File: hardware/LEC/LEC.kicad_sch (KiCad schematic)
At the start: 32 parts, among them J1 54-00278, J10 Conn_01x02, J11 54-00278, J12 54-00278, J13 54-00278, J2 54-00278, J3 54-00278, J4 54-00278, J5 54-00278, J6 54-00278, J7 54-00278, J8 54-00278, J9 54-00278, J9 Conn_01x02, U1 Pico, U15 MCP3564RT-E/ST, U3 MC7809CTG, U4 W25Q128JVSIQ, U5 MAX31855KASA, U6 MAX31855KASA, U7 L7805

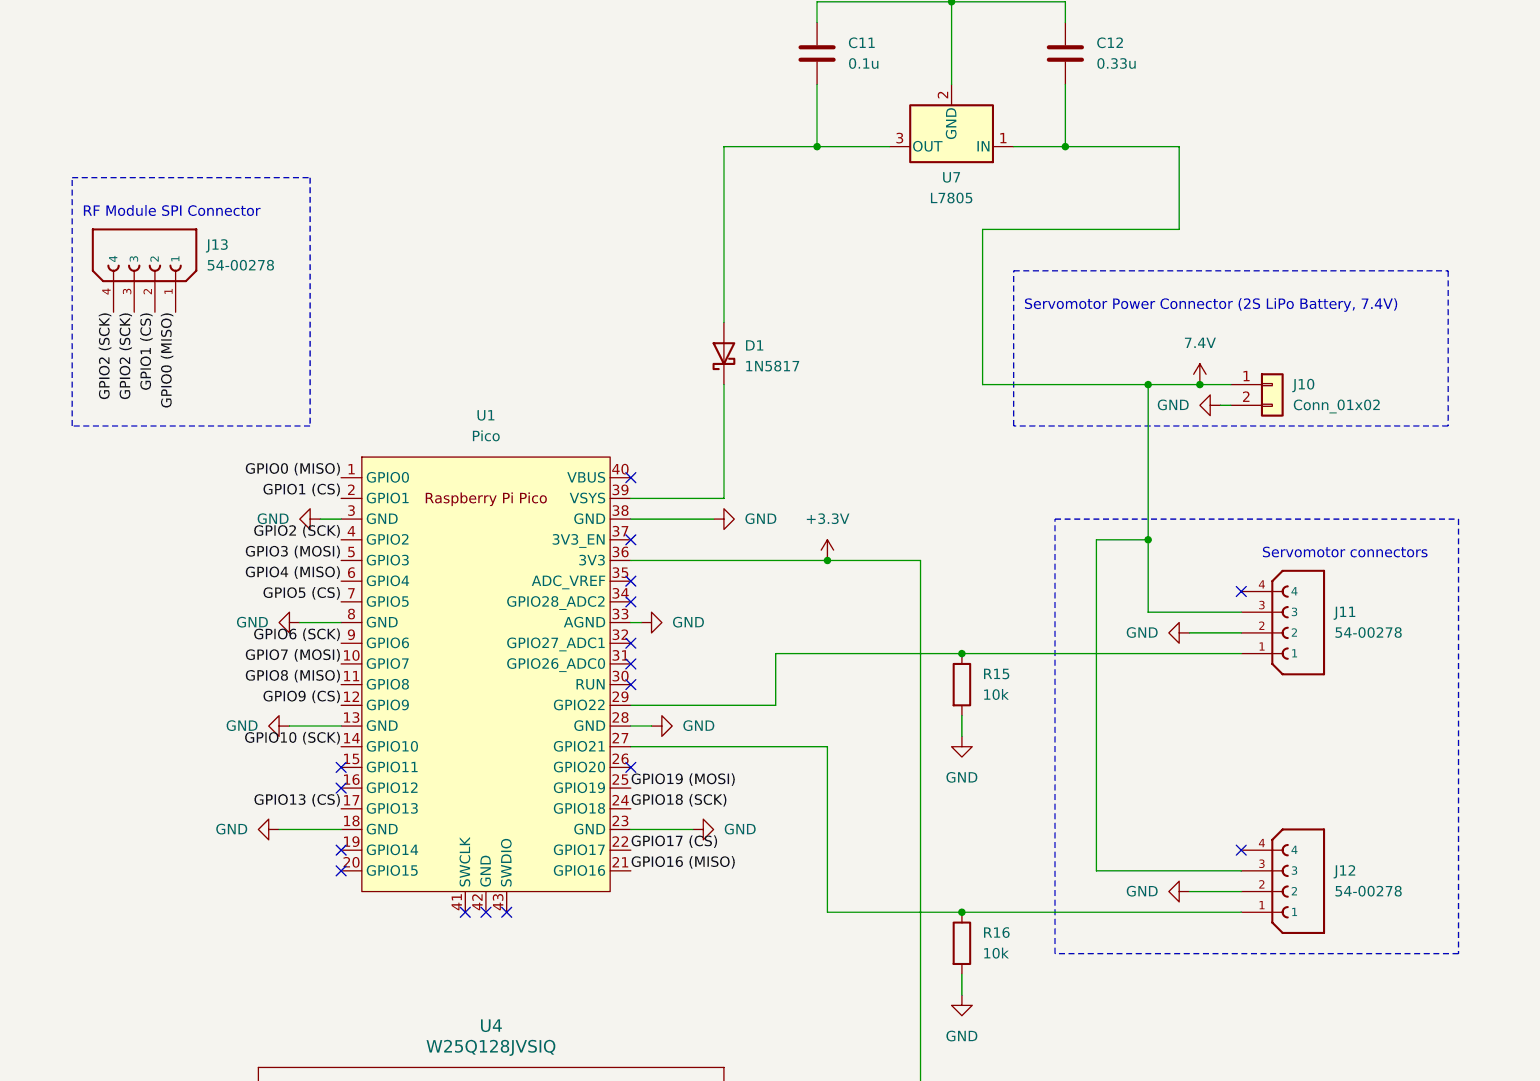
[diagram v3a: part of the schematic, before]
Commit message: Added bulk capacitors to ADC LVRs, servos, and pico power inputs
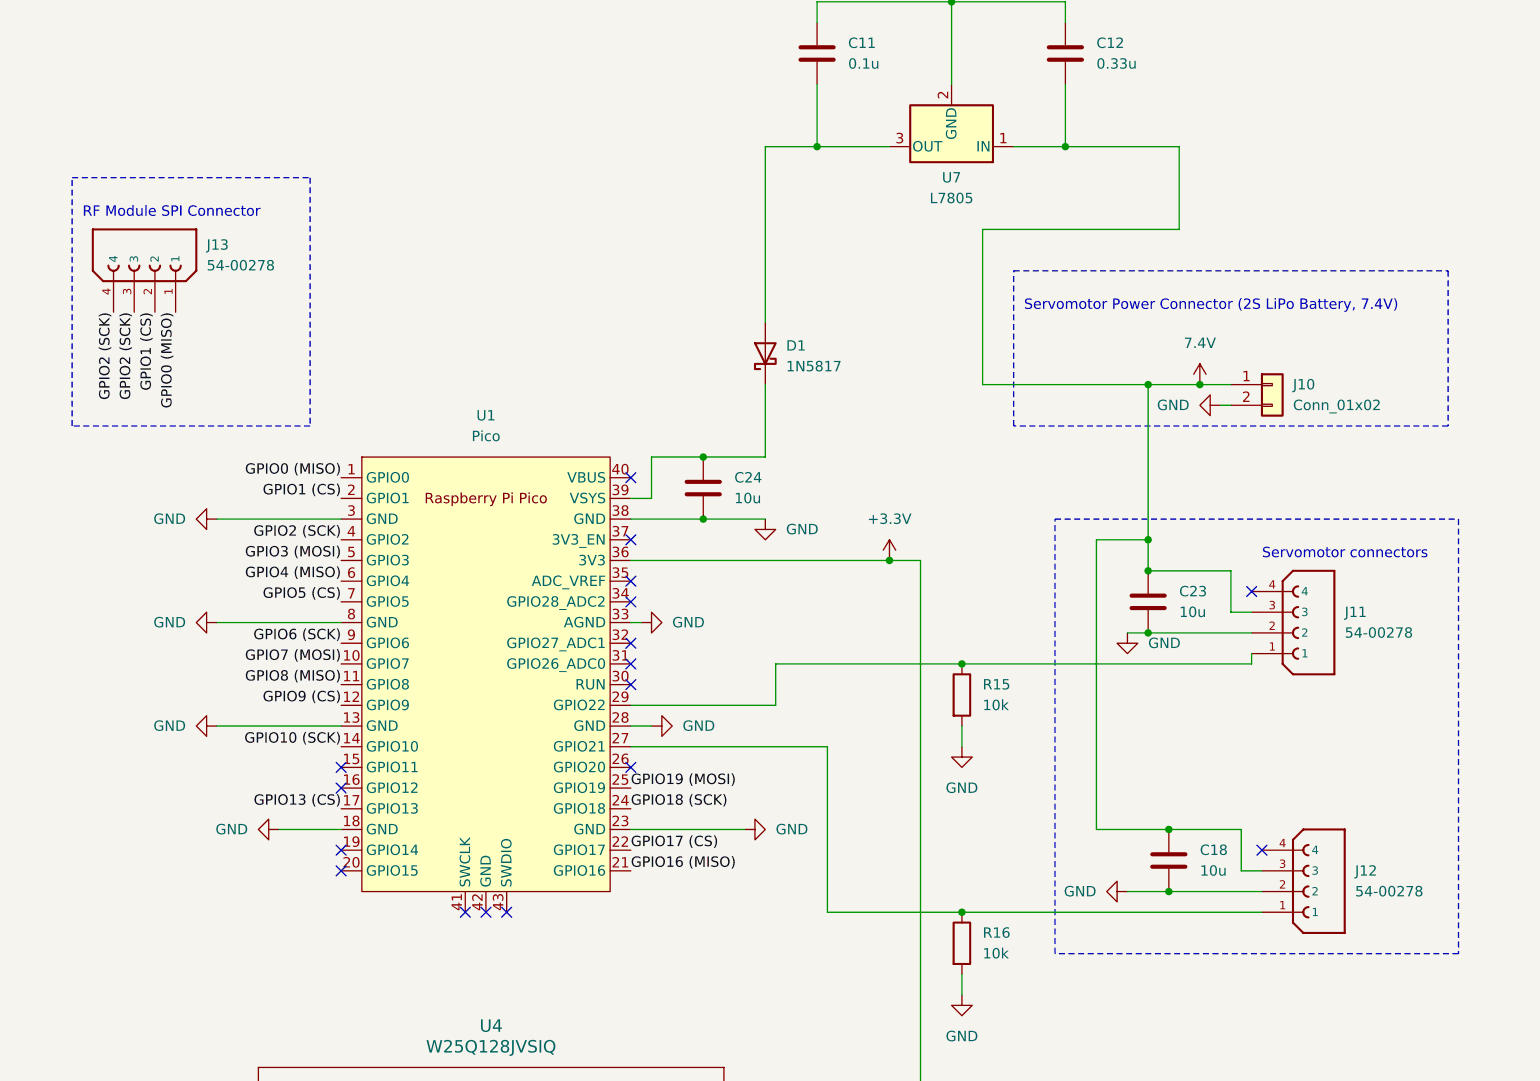
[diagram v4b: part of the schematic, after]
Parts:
- added C18, C23, C24: 10u, symbol Device:C
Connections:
- net +12V: now also C18.1, C23.1
- net GND: now also C18.2, C23.2, C24.2
- net at D1.1 (K), U1.39 (VSYS): now also C24.1
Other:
- moved on the sheet: D1, J11, J12, R15

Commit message: Schematic done
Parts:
- removed C1 (x2): 100n, Capacitor_SMD:C_1206_3216Metric, symbol Device:C
- removed C11: 0.1u, symbol Device:C
- removed C12: 0.33u, symbol Device:C
- removed C23: 10u, symbol Device:C
- removed J9: 54-00278, TENSILITY_54-00278, symbol 4_Pin_M8_Socket_Female:54-00278
- removed R15, R16: 10k, symbol Device:R
- added C1 (x2): 100n, Capacitor_SMD:C_0603_1608Metric, symbol Device:C
- added C21, C22, C25: 10u, Capacitor_SMD:C_0805_2012Metric, symbol Device:C
- added J14: 54-00278, M8Connector:TENSILITY_54-00278, symbol 4_Pin_M8_Socket_Female:54-00278
- added R3 (x2): 10K, Resistor_SMD:R_0603_1608Metric, symbol Device:R_US
- C1: footprint Capacitor_SMD:C_1206_3216Metric -> Capacitor_SMD:C_0603_1608Metric; Digikey https://www.digikey.com/en/products/detail/murata-electroni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 -> https://www.digikey.com/en/products/detail/samsung-electro-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
- C14, C18, C24: footprint (none) -> Capacitor_SMD:C_0805_2012Metric; DigiKey (none) -> https://www.digikey.com/en/products/detail/samsung-electro-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
- C19, C20: value 0.33u -> 10u; footprint (none) -> Capacitor_SMD:C_0805_2012Metric; DigiKey (none) -> https://www.digikey.com/en/products/detail/samsung-electro-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
- J1, J11, J12, J13, J2, J3, J4, J5, J6, J7, J8: footprint TENSILITY_54-00278 -> M8Connector:TENSILITY_54-00278; DigiKey (none) -> https://www.digikey.com/en/products/detail/tensility-intern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
- J10, J9: footprint (none) -> Connector_AMASS:AMASS_XT30UPB-M_1x02_P5.0mm_Vertical
- U1: footprint RPi_Pico:RPi_Pico_SMD_TH -> RPiPico:RPi_Pico_SMD_TH; DigiKey (none) -> https://www.digikey.com/en/products/detail/raspberry-pi/SC0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
- U15: footprint TSSOP20_ST_MCH -> MCP3564R/T:TSSOP20_ST_MCH
- U3: footprint TO-220AB_ONS -> MC7809CTG:TO-220AB_ONS
- U4: footprint SOIC_128JVSIQ_WIN -> W25Q128JVSIQ:SOIC_128JVSIQ_WIN
- U7: footprint (none) -> L7805CV:TO-220_STM; DigiKey (none) -> https://www.digikey.com/en/products/detail/stmicroelectroni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
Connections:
- net +12V: now also J10.2 (Pin_2), C22.1, C25.2; no longer J10.1 (Pin_1)
- net +3.3V: now also C1.1, C1.2
- net ADC_Power_Circuit/VIN: now also J9.2 (Pin_2); no longer J9.1 (Pin_1)
- net GND: now also J10.1 (Pin_1), J9.1 (Pin_1), U1.42 (GND), C1.1, C1.2, C21.1, C22.2, C25.1, R3.2, R3.2; no longer J10.2 (Pin_2), J9.2 (Pin_2)
- net at J12.1, U1.27 (GPIO21): now also R3.1
- net at J11.1, U1.29 (GPIO22): now also R3.1
- net at D1.2 (A), U7.3 (OUT): now also C21.2
- net at U5.3 (T+): now also J14.1
- net at U5.2 (T-): now also J14.2
- no-connect marks 24 -> 23

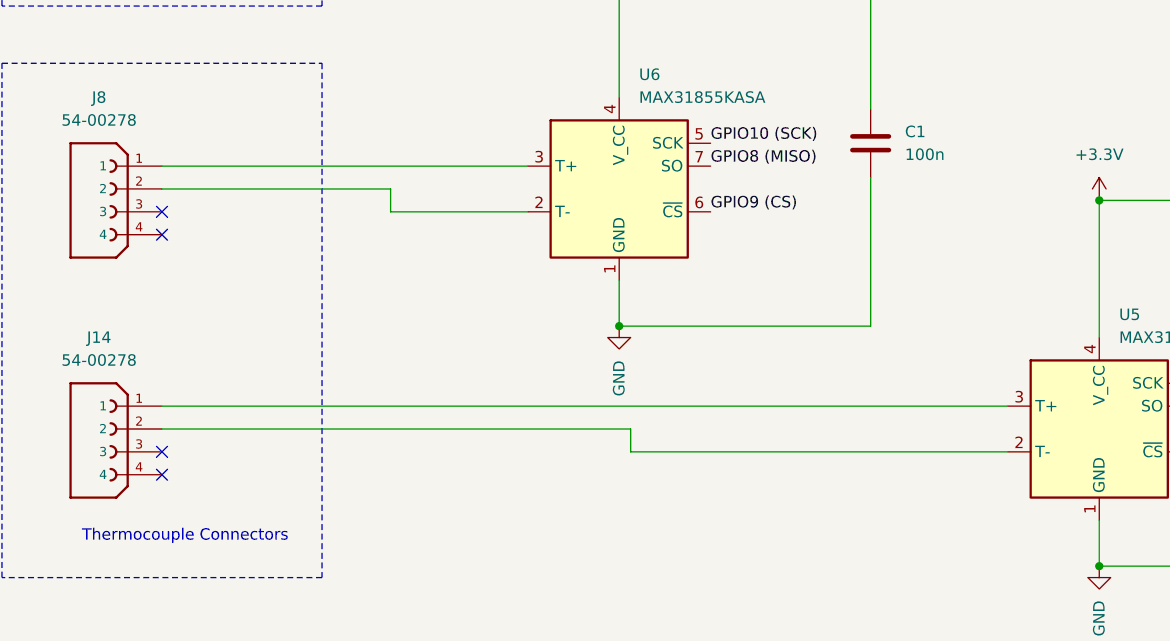
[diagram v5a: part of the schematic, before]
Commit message: Added decoupling capacitor across thermocouple inputs
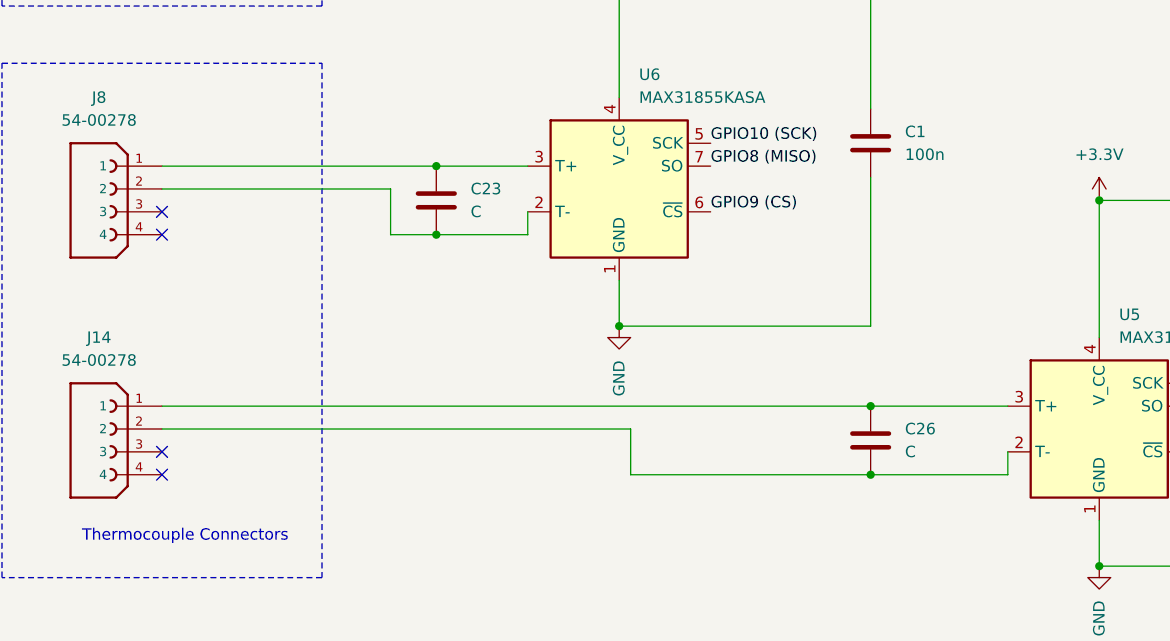
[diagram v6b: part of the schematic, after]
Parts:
- added C23, C26: C, Capacitor_SMD:C_0603_1608Metric, symbol Device:C
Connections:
- net at J14.1, U5.3 (T+): now also C26.1
- net at J14.2, U5.2 (T-): now also C26.2
- net at J8.2, U6.2 (T-): now also C23.2
- net at J8.1, U6.3 (T+): now also C23.1
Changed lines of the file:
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@@
     (comment 1 "Designer: Rakshak Sudhakaran")
   )
+  (junction (at 127 254) (diameter 0) (color 0 0 0 0)
+  )
   (junction (at 340.36 224.79) (diameter 0) (color 0 0 0 0)
   )
   (junction (at 104.14 140.97) (diameter 0) (color 0 0 0 0)
   )
+  (junction (at 78.74 227.33) (diameter 0) (color 0 0 0 0)
+  )
   (junction (at 187.96 72.39) (diameter 0) (color 0 0 0 0)
   )
@@
   (junction (at 251.46 240.03) (diameter 0) (color 0 0 0 0)
   )
+  (junction (at 78.74 234.95) (diameter 0) (color 0 0 0 0)
+  )
   (junction (at 314.96 142.24) (diameter 0) (color 0 0 0 0)
+  )
+  (junction (at 127 261.62) (diameter 0) (color 0 0 0 0)
   )
   (junction (at 251.46 229.87) (diameter 0) (color 0 0 0 0)
@@
     (stroke (width 0) (type default))
   )
-  (wire (pts (xy 73.66 232.41) (xy 88.9 232.41))
+  (wire (pts (xy 73.66 234.95) (xy 78.74 234.95))
     (stroke (width 0) (type default))
   )
@@
     (stroke (width 0) (type default))
   )
-  (wire (pts (xy 73.66 229.87) (xy 73.66 232.41))
+  (wire (pts (xy 73.66 229.87) (xy 73.66 234.95))
     (stroke (width 0) (type default))
   )
@@
     (stroke (width 0) (type default))
   )
-  (wire (pts (xy 48.26 227.33) (xy 88.9 227.33))
+  (wire (pts (xy 48.26 227.33) (xy 78.74 227.33))
     (stroke (width 0) (type default))
   )
@@
     (stroke (width 0) (type default))
   )
+  (wire (pts (xy 78.74 234.95) (xy 88.9 234.95))
+    (stroke (width 0) (type default))
+  )
   (wire (pts (xy 370.84 195.58) (xy 382.27 195.58))
     (stroke (width 0) (type default))
   )
-  (wire (pts (xy 100.33 259.08) (xy 142.24 259.08))
+  (wire (pts (xy 100.33 261.62) (xy 127 261.62))
     (stroke (width 0) (type default))
   )
@@
     (stroke (width 0) (type default))
   )
-  (wire (pts (xy 48.26 254) (xy 142.24 254))
+  (wire (pts (xy 142.24 261.62) (xy 142.24 259.08))
+    (stroke (width 0) (type default))
+  )
+  (wire (pts (xy 48.26 254) (xy 127 254))
     (stroke (width 0) (type default))
   )
@@
     (stroke (width 0) (type default))
   )
+  (wire (pts (xy 78.74 227.33) (xy 88.9 227.33))
+    (stroke (width 0) (type default))
+  )
   (wire (pts (xy 130.81 41.91) (xy 104.14 41.91))
     (stroke (width 0) (type default))
@@
     (stroke (width 0) (type default))
   )
-  (wire (pts (xy 100.33 256.54) (xy 100.33 259.08))
+  (wire (pts (xy 100.33 256.54) (xy 100.33 261.62))
     (stroke (width 0) (type default))
   )
@@
     (stroke (width 0) (type default))
   )
+  (wire (pts (xy 127 254) (xy 142.24 254))
+    (stroke (width 0) (type default))
+  )
   (wire (pts (xy 115.57 171.45) (xy 144.78 171.45))
     (stroke (width 0) (type default))
@@
     (stroke (width 0) (type default))
   )
+  (wire (pts (xy 88.9 234.95) (xy 88.9 232.41))
+    (stroke (width 0) (type default))
+  )
   (wire (pts (xy 304.8 162.56) (xy 306.07 162.56))
     (stroke (width 0) (type default))
@@
   )
   (wire (pts (xy 152.4 231.14) (xy 152.4 246.38))
+    (stroke (width 0) (type default))
+  )
+  (wire (pts (xy 127 261.62) (xy 142.24 261.62))
     (stroke (width 0) (type default))
   )
@@
     )
   )
+  (symbol (lib_id "Device:C") (at 78.74 231.14 0) (unit 1)
+    (in_bom yes) (on_board yes) (dnp no) (fields_autoplaced)
+    (property "Reference" "C23" (at 82.55 229.87 0)
+      (effects (font (size 1.27 1.27)) (justify left))
+    )
+    (property "Value" "C" (at 82.55 232.41 0)
+      (effects (font (size 1.27 1.27)) (justify left))
+    )
+    (property "Footprint" "Capacitor_SMD:C_0603_1608Metric" (at 79.7052 234.95 0)
+      (effects (font (size 1.27 1.27)) hide)
+    )
+    (property "Datasheet" "https://search.murata.co.jp/Ceramy/image/img/A01X/G101/ENG/GRM1885C1H103JA01-01.pdf" (at 78.74 231.14 0)
+      (effects (font (size 1.27 1.27)) hide)
+    )
+    (property "DigiKey" "https://www.digikey.com/en/products/detail/murata-electronics/GRM1885C1H103JA01D/4421555" (at 78.74 231.14 0)
+      (effects (font (size 1.27 1.27)) hide)
+    )
+    (pin "1")
+    (pin "2")
+    (instances
+      (project "LEC"
+        (path "/c984ce56-a2b4-4cda-8793-153280694173"
+          (reference "C23") (unit 1)
+        )
+      )
+    )
+  )
   (symbol (lib_id "power:+3.3V") (at 152.4 231.14 0) (unit 1)
     (in_bom yes) (on_board yes) (dnp no) (fields_autoplaced)
@@
         )
       )
+    )
+  )
+  (symbol (lib_id "Device:C") (at 127 257.81 0) (unit 1)
+    (in_bom yes) (on_board yes) (dnp no) (fields_autoplaced)
+    (property "Reference" "C26" (at 130.81 256.54 0)
+      (effects (font (size 1.27 1.27)) (justify left))
+    )
+    (property "Value" "C" (at 130.81 259.08 0)
+      (effects (font (size 1.27 1.27)) (justify left))
+    )
+    (property "Footprint" "Capacitor_SMD:C_0603_1608Metric" (at 127.9652 261.62 0)
+      (effects (font (size 1.27 1.27)) hide)
+    )
+    (property "Datasheet" "https://search.murata.co.jp/Ceramy/image/img/A01X/G101/ENG/GRM1885C1H103JA01-01.pdf" (at 127 257.81 0)
+      (effects (font (size 1.27 1.27)) hide)
+    )
+    (property "DigiKey" "https://www.digikey.com/en/products/detail/murata-electronics/GRM1885C1H103JA01D/4421555" (at 127 257.81 0)
+      (effects (font (size 1.27 1.27)) hide)
+    )
+    (pin "1")
+    (pin "2")
+    (instances
+      (project "LEC"
+        (path "/c984ce56-a2b4-4cda-8793-153280694173"
+          (reference "C26") (unit 1)
+        )
+      )
